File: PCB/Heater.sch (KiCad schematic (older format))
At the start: 50 parts, among them IC1 ATTINY45-P, J1 GND, J2 RST, P1 220V 50Hz, P2 CONN_01X04, P3 DS18B20, U1 MOC3023M

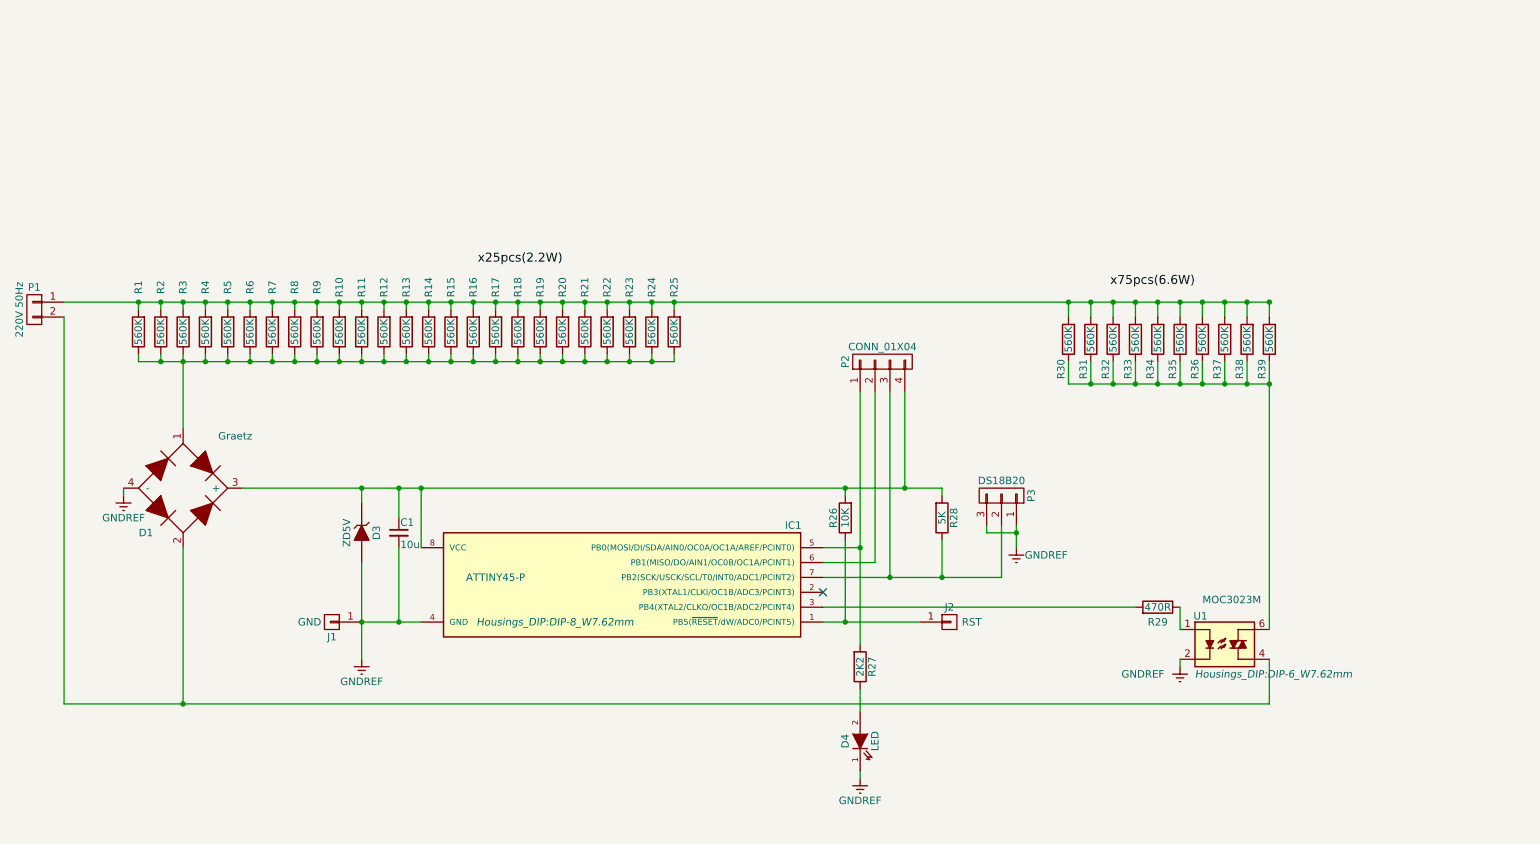
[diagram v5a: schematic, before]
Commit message: new design with stronger resistors
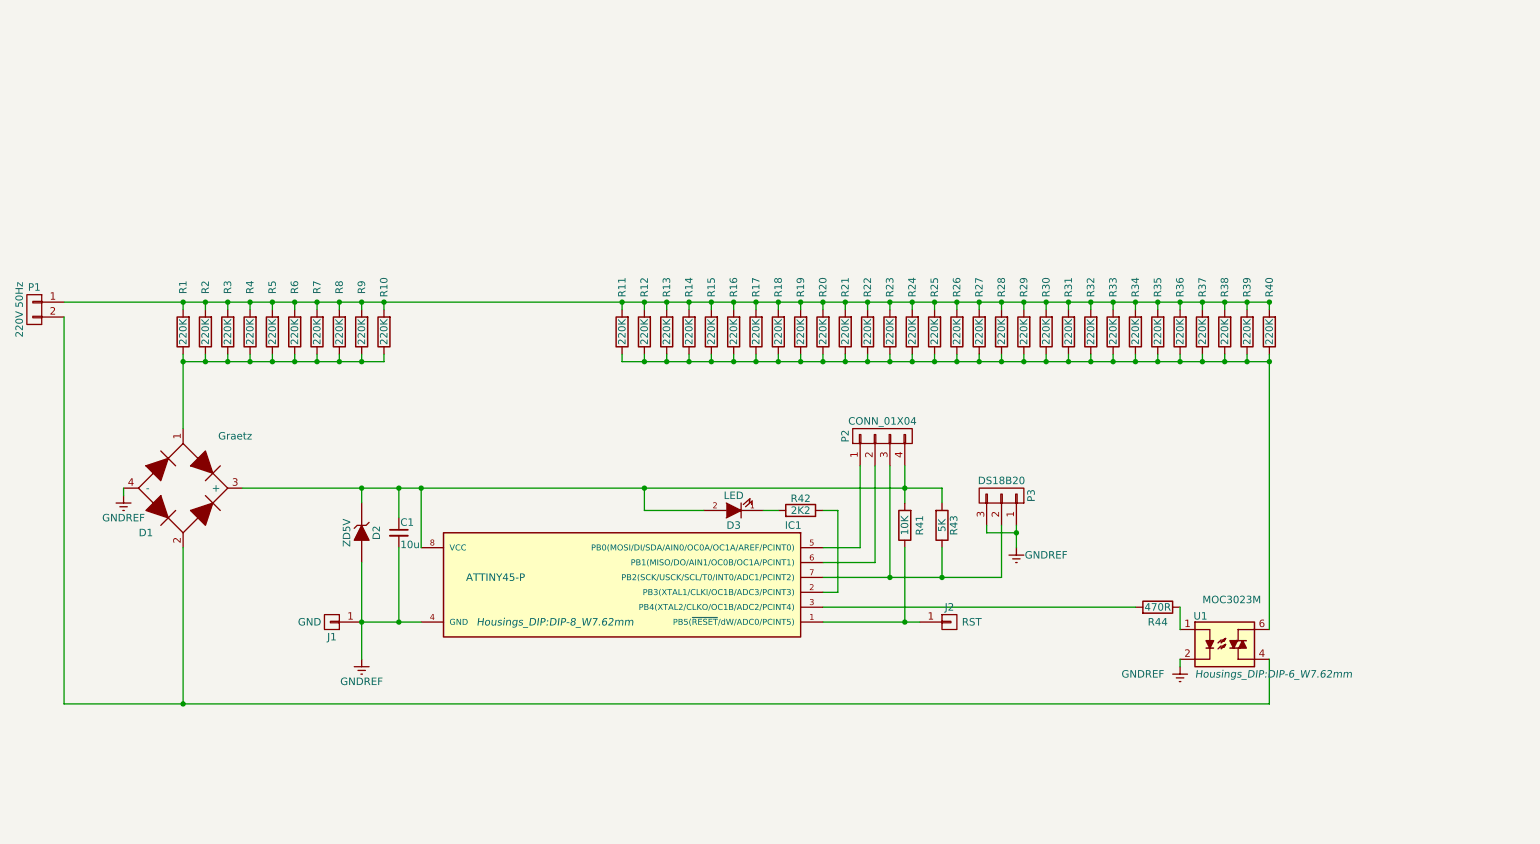
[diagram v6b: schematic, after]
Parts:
- added R26, R27, R28, R29, R40: 220K, Resistors_SMD:R_1210, symbol R
- R1, R10, R11, R12, R13, R14, R15, R16, R17, R18, R19, R2, R20, R21, R22, R23, R24, R25, R3, R30, R31, R32, R33, R34, R35, R36, R37, R38, R39, R4, R5, R6, R7, R8, R9: value 560K -> 220K; footprint Resistors_SMD:R_0805 -> Resistors_SMD:R_1210
- renumbered D3 to D2, D4 to D3, R26 to R41, R27 to R42, R28 to R43, R29 to R44
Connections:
- net GNDREF: no longer D3.1 (K)
- net at IC1.2 (PB3(XTAL1/CLKI/OC1B/ADC3/PCINT3)): now also R42.1
- net at IC1.5 (PB0(MOSI/DI/SDA/AIN0/OC0A/OC1A/AREF/PCINT0)), P2.1 (P1): no longer R42.2
- net at C1.1, D1.3 (+), D2.1 (K)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: now also D3.2 (A)
- net at R11.1, R12.1, R13.1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: now also R30.1, R31.1, R32.1, R33.1, R34.1, R35.1, R36.1, R37.1, R38.1, R39.1, U1.6, R26.1, R27.1, R28.1, R29.1, R40.1; no longer D1.1, R1.1, R10.1, R2.1, R3.1, R4.1, R5.1, R6.1, R7.1, R8.1, R9.1
- net at P1.1 (P1), R1.2, R10.2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: now also R26.2, R27.2, R28.2, R29.2, R40.2
- new net: D1.1, R1.1, R10.1, R2.1, R3.1, R4.1, R5.1, R6.1, R7.1, R8.1, R9.1
- new net: D3.1 (K), R42.2
- no-connect marks 1 -> 0
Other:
- moved on the sheet: D3, P2, R41, R42, R43
